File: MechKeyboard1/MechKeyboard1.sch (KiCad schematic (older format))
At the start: 21 parts, among them J1 AVR-ISP-6, SW1 SW_Push_Reset, U1 ATmega32U4-AU, U2 PRTR5V0U2X, X1 XTAL

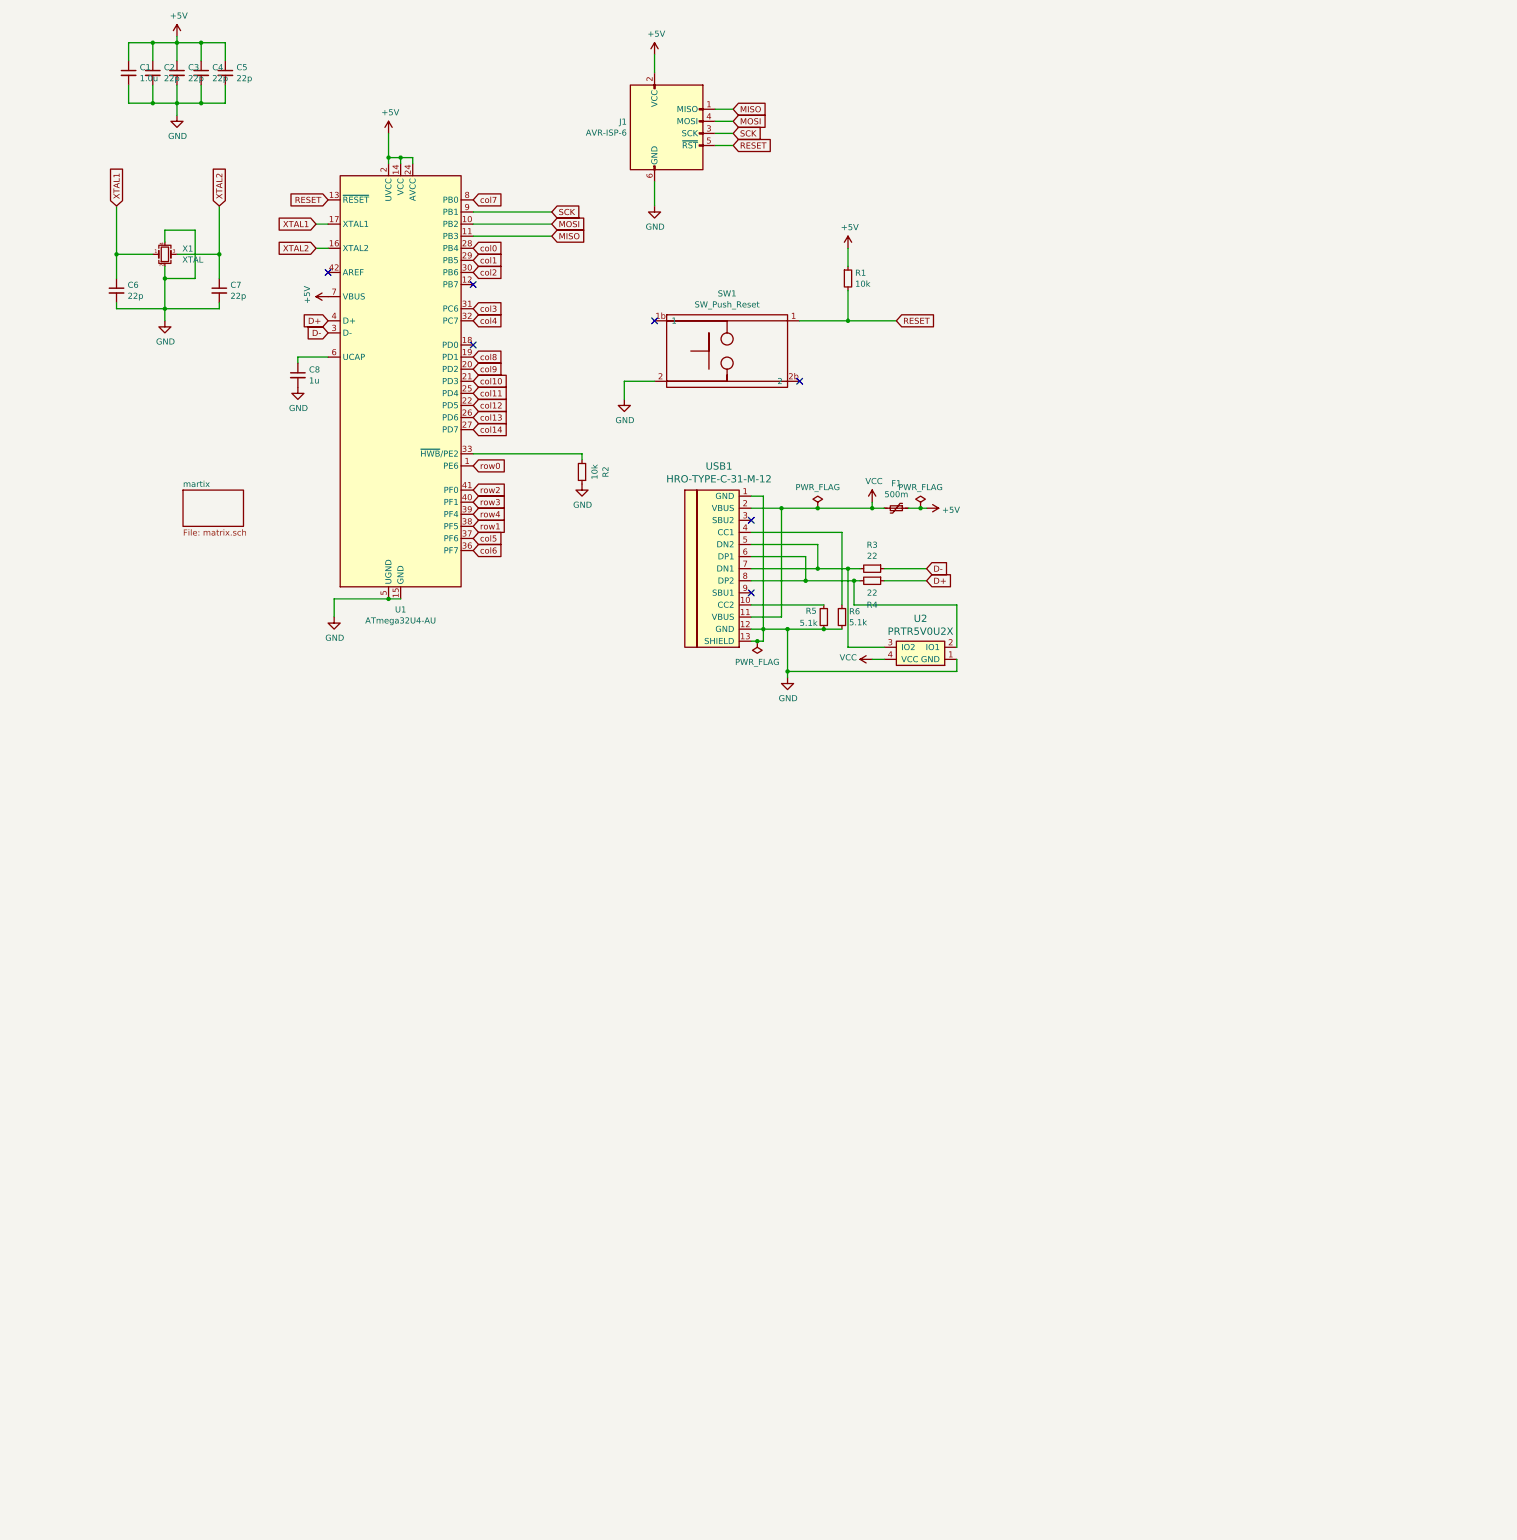
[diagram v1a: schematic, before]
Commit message: Learned Matrix, Annotate, Footprints, & Render Components
*Removed Matrix (caused errors)
*Created Custom Symbols
*Assigned Keys & Layouts
*Rendered Footprints
*Learned Cutting Edges for PCB
*3D Rendered PCB
*Placed ICs to prepare Routing
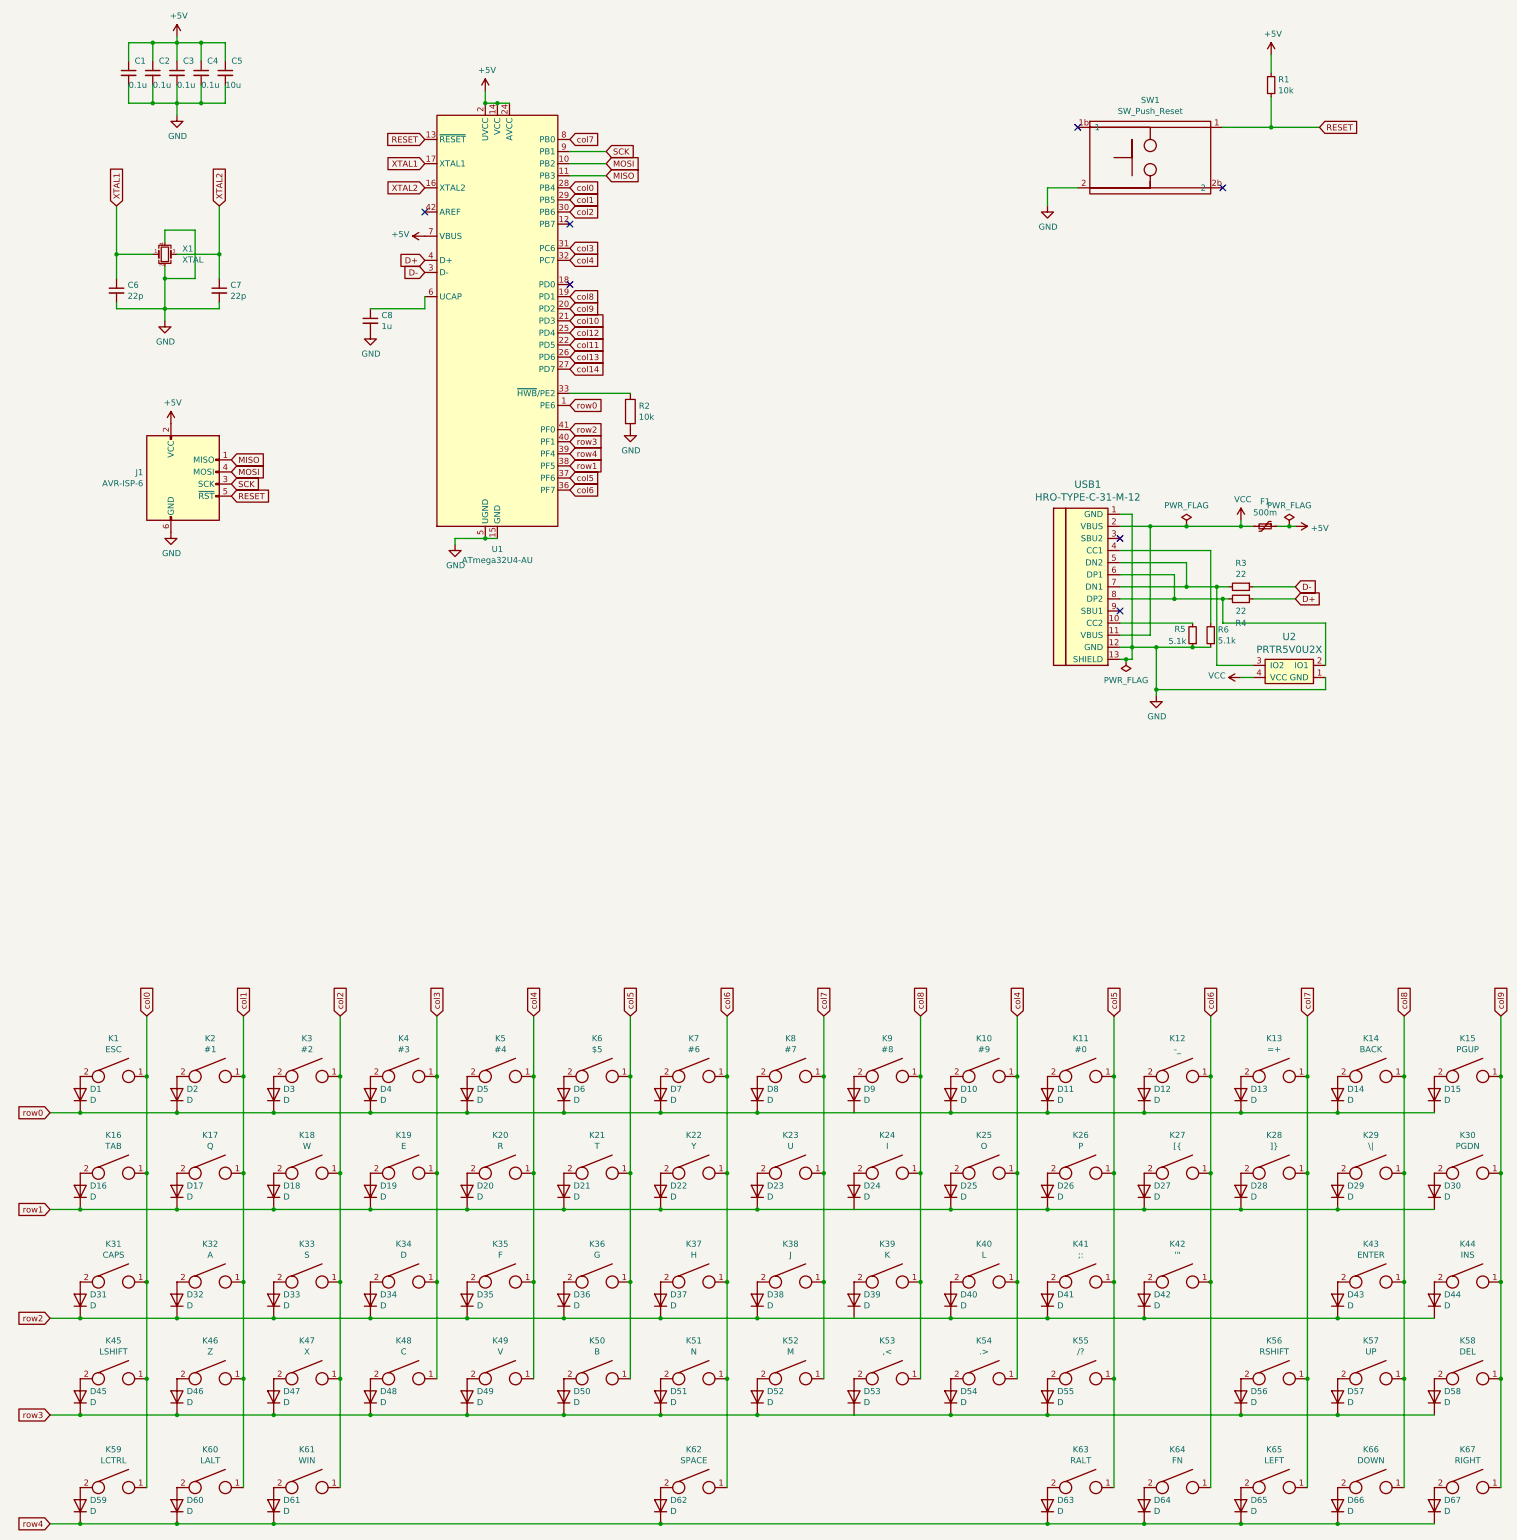
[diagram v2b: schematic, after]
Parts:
- removed R2: 10k, symbol Device:R_Small
- added D1, D10, D11, D12, D13, D14, D15, D16, D17, D18, D19, D2, D20, D21, D22, D23, D24, D25, D26, D27, D28, D29, D3, D30, D31, D32, D33, D34, D35, D36, D37, D38, D39, D4, D40, D41, D42, D43, D44, D45, D46, D47, D48, D49, D5, D50, D51, D52, D53, D54, D55, D56, D57, D58, D59, D6, D60, D61, D62, D63, D64, D65, D66, D67, D7, D8, D9: D, Diode_SMD:D_0805_2012Metric_Pad1.15x1.40mm_HandSolder, symbol Device:D
- added K1: ESC, Alps_Only:ALPS-1U, symbol Switch:SW_Push2
- added K10: #9, Alps_Only:ALPS-1U, symbol Switch:SW_Push2
- added K11: #0, Alps_Only:ALPS-1U, symbol Switch:SW_Push2
- added K12: -_, Alps_Only:ALPS-1U, symbol Switch:SW_Push2
- added K13: =+, Alps_Only:ALPS-1U, symbol Switch:SW_Push2
- added K14: BACK, Alps_Only:ALPS-2U, symbol Switch:SW_Push2
- added K15: PGUP, Alps_Only:ALPS-1U, symbol Switch:SW_Push2
- added K16: TAB, Alps_Only:ALPS-1.5U, symbol Switch:SW_Push2
- added K17: Q, Alps_Only:ALPS-1U, symbol Switch:SW_Push2
- added K18: W, Alps_Only:ALPS-1U, symbol Switch:SW_Push2
- added K19: E, Alps_Only:ALPS-1U, symbol Switch:SW_Push2
- added K2: #1, Alps_Only:ALPS-1U, symbol Switch:SW_Push2
- added K20: R, Alps_Only:ALPS-1U, symbol Switch:SW_Push2
- added K21: T, Alps_Only:ALPS-1U, symbol Switch:SW_Push2
- added K22: Y, Alps_Only:ALPS-1U, symbol Switch:SW_Push2
- added K23: U, Alps_Only:ALPS-1U, symbol Switch:SW_Push2
- added K24: I, Alps_Only:ALPS-1U, symbol Switch:SW_Push2
- added K25: O, Alps_Only:ALPS-1U, symbol Switch:SW_Push2
- added K26: P, Alps_Only:ALPS-1U, symbol Switch:SW_Push2
- added K27: [{, Alps_Only:ALPS-1U, symbol Switch:SW_Push2
- added K28: ]}, Alps_Only:ALPS-1U, symbol Switch:SW_Push2
- added K29: \\|, Alps_Only:ALPS-1.5U, symbol Switch:SW_Push2
- added K3: #2, Alps_Only:ALPS-1U, symbol Switch:SW_Push2
- added K30: PGDN, Alps_Only:ALPS-1U, symbol Switch:SW_Push2
- added K31: CAPS, Alps_Only:ALPS-1.75U, symbol Switch:SW_Push2
- added K32: A, Alps_Only:ALPS-1U, symbol Switch:SW_Push2
- added K33: S, Alps_Only:ALPS-1U, symbol Switch:SW_Push2
- added K34: D, Alps_Only:ALPS-1U, symbol Switch:SW_Push2
- added K35: F, Alps_Only:ALPS-1U, symbol Switch:SW_Push2
- added K36: G, Alps_Only:ALPS-1U, symbol Switch:SW_Push2
- added K37: H, Alps_Only:ALPS-1U, symbol Switch:SW_Push2
- added K38: J, Alps_Only:ALPS-1U, symbol Switch:SW_Push2
- added K39: K, Alps_Only:ALPS-1U, symbol Switch:SW_Push2
- added K4: #3, Alps_Only:ALPS-1U, symbol Switch:SW_Push2
- added K40: L, Alps_Only:ALPS-1U, symbol Switch:SW_Push2
- added K41: ;:, Alps_Only:ALPS-1U, symbol Switch:SW_Push2
- added K42: '\", Alps_Only:ALPS-1U, symbol Switch:SW_Push2
- added K43: ENTER, Alps_Only:ALPS-2.25U, symbol Switch:SW_Push2
- added K44: INS, Alps_Only:ALPS-1U, symbol Switch:SW_Push2
- added K45: LSHIFT, Alps_Only:ALPS-2.25U, symbol Switch:SW_Push2
- added K46: Z, Alps_Only:ALPS-1U, symbol Switch:SW_Push2
- added K47: X, Alps_Only:ALPS-1U, symbol Switch:SW_Push2
- added K48: C, Alps_Only:ALPS-1U, symbol Switch:SW_Push2
- added K49: V, Alps_Only:ALPS-1U, symbol Switch:SW_Push2
- added K5: #4, Alps_Only:ALPS-1U, symbol Switch:SW_Push2
- added K50: B, Alps_Only:ALPS-1U, symbol Switch:SW_Push2
- added K51: N, Alps_Only:ALPS-1U, symbol Switch:SW_Push2
- added K52: M, Alps_Only:ALPS-1U, symbol Switch:SW_Push2
- added K53: ,<, Alps_Only:ALPS-1U, symbol Switch:SW_Push2
- added K54: .>, Alps_Only:ALPS-1U, symbol Switch:SW_Push2
- added K55: /?, Alps_Only:ALPS-1U, symbol Switch:SW_Push2
- added K56: RSHIFT, Alps_Only:ALPS-1.75U, symbol Switch:SW_Push2
- added K57: UP, Alps_Only:ALPS-1U, symbol Switch:SW_Push2
- added K58: DEL, Alps_Only:ALPS-1U, symbol Switch:SW_Push2
- added K59: LCTRL, Alps_Only:ALPS-1.5U, symbol Switch:SW_Push2
- added K6: $5, Alps_Only:ALPS-1U, symbol Switch:SW_Push2
- added K60: LALT, Alps_Only:ALPS-1.25U, symbol Switch:SW_Push2
- added K61: WIN, Alps_Only:ALPS-1.5U, symbol Switch:SW_Push2
- added K62: SPACE, Alps_Only:ALPS-6.5U, symbol Switch:SW_Push2
- added K63: RALT, Alps_Only:ALPS-1.25U, symbol Switch:SW_Push2
- added K64: FN, Alps_Only:ALPS-1U, symbol Switch:SW_Push2
- added K65: LEFT, Alps_Only:ALPS-1U, symbol Switch:SW_Push2
- added K66: DOWN, Alps_Only:ALPS-1U, symbol Switch:SW_Push2
- added K67: RIGHT, Alps_Only:ALPS-1U, symbol Switch:SW_Push2
- added K7: #6, Alps_Only:ALPS-1U, symbol Switch:SW_Push2
- added K8: #7, Alps_Only:ALPS-1U, symbol Switch:SW_Push2
- added K9: #8, Alps_Only:ALPS-1U, symbol Switch:SW_Push2
- added R2: 10k, Resistor_SMD:R_0805_2012Metric_Pad1.20x1.40mm_HandSolder, symbol Device:R
- C1: value 1.0u -> 0.1u; footprint (none) -> Capacitor_SMD:C_0805_2012Metric_Pad1.18x1.45mm_HandSolder
- C2, C3, C4: value 22p -> 0.1u; footprint (none) -> Capacitor_SMD:C_0805_2012Metric_Pad1.18x1.45mm_HandSolder
- C5: value 22p -> 10u; footprint (none) -> Capacitor_SMD:C_0805_2012Metric_Pad1.18x1.45mm_HandSolder
- C6, C7, C8: footprint (none) -> Capacitor_SMD:C_0805_2012Metric_Pad1.18x1.45mm_HandSolder
- F1: footprint (none) -> Fuse:Fuse_1206_3216Metric_Pad1.42x1.75mm_HandSolder
- J1: footprint (none) -> random-keyboard-parts:Reset_Pretty-Mask
- R1, R3, R4, R5, R6: footprint (none) -> Resistor_SMD:R_0805_2012Metric_Pad1.20x1.40mm_HandSolder
- SW1: footprint (none) -> Button_Switch_SMD:SW_SPST_SKQG_WithStem
- U2: footprint (none) -> random-keyboard-parts:SOT143B
- USB1: footprint (none) -> Type-C:HRO-TYPE-C-31-M-12-HandSoldering
- X1: footprint (none) -> Crystal:Crystal_SMD_3225-4Pin_3.2x2.5mm_HandSoldering
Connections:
- net GND: now also R2.2
- net col0: now also K1.1, K16.1, K31.1, K45.1, K59.1
- net col1: now also K17.1, K2.1, K32.1, K46.1, K60.1
- net col11: now also U1.22 (PD5); no longer U1.25 (PD4)
- net col12: now also U1.25 (PD4); no longer U1.22 (PD5)
- net col2: now also K18.1, K3.1, K33.1, K47.1, K61.1
- net col3: now also K19.1, K34.1, K4.1, K48.1
- net col4: now also K10.1, K20.1, K25.1, K35.1, K40.1, K49.1, K5.1, K54.1
- net col5: now also K11.1, K21.1, K26.1, K36.1, K41.1, K50.1, K55.1, K6.1, K63.1
- net col6: now also K12.1, K22.1, K27.1, K37.1, K42.1, K51.1, K62.1, K64.1, K7.1
- net col7: now also K13.1, K23.1, K28.1, K38.1, K52.1, K56.1, K65.1, K8.1
- net col8: now also K14.1, K24.1, K29.1, K39.1, K43.1, K53.1, K57.1, K66.1, K9.1
- net col9: now also K15.1, K30.1, K44.1, K58.1, K67.1
- net row0: now also D1.1 (K), D10.1 (K), D11.1 (K), D12.1 (K), D13.1 (K), D14.1 (K), D15.1 (K), D2.1 (K), D3.1 (K), D4.1 (K), D5.1 (K), D6.1 (K), D7.1 (K), D8.1 (K), D9.1 (K)
- net row1: now also D16.1 (K), D17.1 (K), D18.1 (K), D19.1 (K), D20.1 (K), D21.1 (K), D22.1 (K), D23.1 (K), D24.1 (K), D25.1 (K), D26.1 (K), D27.1 (K), D28.1 (K), D29.1 (K), D30.1 (K)
- net row2: now also D31.1 (K), D32.1 (K), D33.1 (K), D34.1 (K), D35.1 (K), D36.1 (K), D37.1 (K), D38.1 (K), D39.1 (K), D40.1 (K), D41.1 (K), D42.1 (K), D43.1 (K), D44.1 (K)
- net row3: now also D45.1 (K), D46.1 (K), D47.1 (K), D48.1 (K), D49.1 (K), D50.1 (K), D51.1 (K), D52.1 (K), D53.1 (K), D54.1 (K), D55.1 (K), D56.1 (K), D57.1 (K), D58.1 (K)
- net row4: now also D59.1 (K), D60.1 (K), D61.1 (K), D62.1 (K), D63.1 (K), D64.1 (K), D65.1 (K), D66.1 (K), D67.1 (K)
- net at U1.33 (~HWB~/PE2): now also R2.1
- new net: D1.2 (A), K1.2
- new net: D2.2 (A), K2.2
- new net: D3.2 (A), K3.2
- new net: D4.2 (A), K4.2
- new net: D5.2 (A), K5.2
- new net: D16.2 (A), K16.2
- new net: D17.2 (A), K17.2
- new net: D18.2 (A), K18.2
- new net: D19.2 (A), K19.2
- new net: D20.2 (A), K20.2
- new net: D6.2 (A), K6.2
- new net: D7.2 (A), K7.2
- new net: D8.2 (A), K8.2
- new net: D9.2 (A), K9.2
- new net: D15.2 (A), K15.2
- new net: D21.2 (A), K21.2
- new net: D22.2 (A), K22.2
- new net: D23.2 (A), K23.2
- new net: D24.2 (A), K24.2
- new net: D30.2 (A), K30.2
- new net: D31.2 (A), K31.2
- new net: D32.2 (A), K32.2
- new net: D33.2 (A), K33.2
- new net: D34.2 (A), K34.2
- new net: D35.2 (A), K35.2
- new net: D36.2 (A), K36.2
- new net: D37.2 (A), K37.2
- new net: D38.2 (A), K38.2
- new net: D39.2 (A), K39.2
- new net: D44.2 (A), K44.2
- new net: D45.2 (A), K45.2
- new net: D46.2 (A), K46.2
- new net: D47.2 (A), K47.2
- new net: D48.2 (A), K48.2
- new net: D49.2 (A), K49.2
- new net: D50.2 (A), K50.2
- new net: D51.2 (A), K51.2
- new net: D52.2 (A), K52.2
- new net: D53.2 (A), K53.2
- new net: D58.2 (A), K58.2
- new net: D59.2 (A), K59.2
- new net: D60.2 (A), K60.2
- new net: D61.2 (A), K61.2
- new net: D62.2 (A), K62.2
- new net: D67.2 (A), K67.2
- new net: D10.2 (A), K10.2
- new net: D25.2 (A), K25.2
- new net: D11.2 (A), K11.2
- new net: D12.2 (A), K12.2
- new net: D13.2 (A), K13.2
- new net: D14.2 (A), K14.2
- new net: D26.2 (A), K26.2
- new net: D27.2 (A), K27.2
- new net: D28.2 (A), K28.2
- new net: D29.2 (A), K29.2
- new net: D40.2 (A), K40.2
- new net: D41.2 (A), K41.2
- new net: D42.2 (A), K42.2
- new net: D43.2 (A), K43.2
- new net: D54.2 (A), K54.2
- new net: D55.2 (A), K55.2
- new net: D56.2 (A), K56.2
- new net: D57.2 (A), K57.2
- new net: D63.2 (A), K63.2
- new net: D64.2 (A), K64.2
- new net: D65.2 (A), K65.2
- new net: D66.2 (A), K66.2
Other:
- moved on the sheet: F1, J1, R1, R3, R4, R5, R6, SW1, U2, USB1
